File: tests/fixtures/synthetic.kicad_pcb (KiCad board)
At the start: 2 copper layers, 50 x 30 mm, 3 parts, among them U1 REG

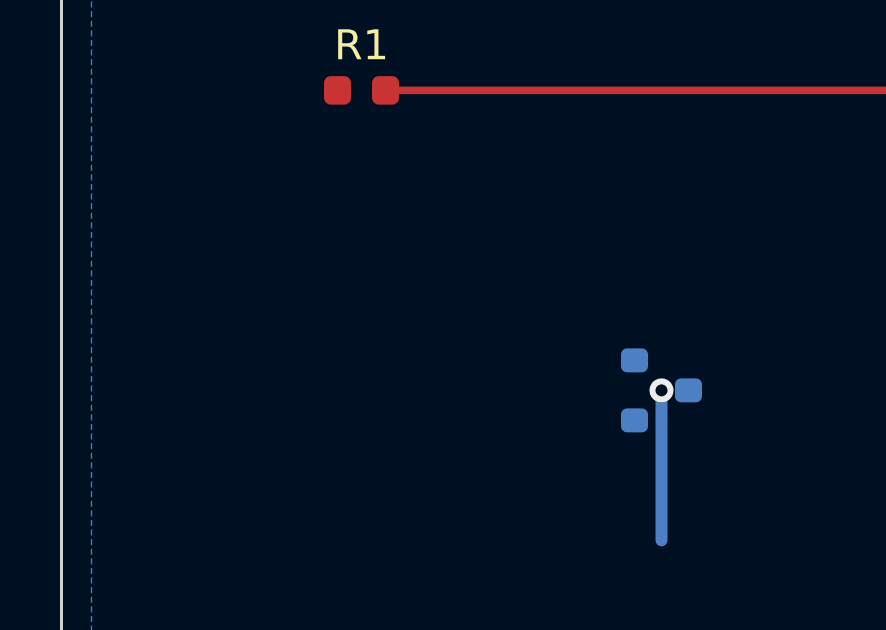
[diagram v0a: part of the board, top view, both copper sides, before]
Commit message: [Build] fix synthetic route fixture edits
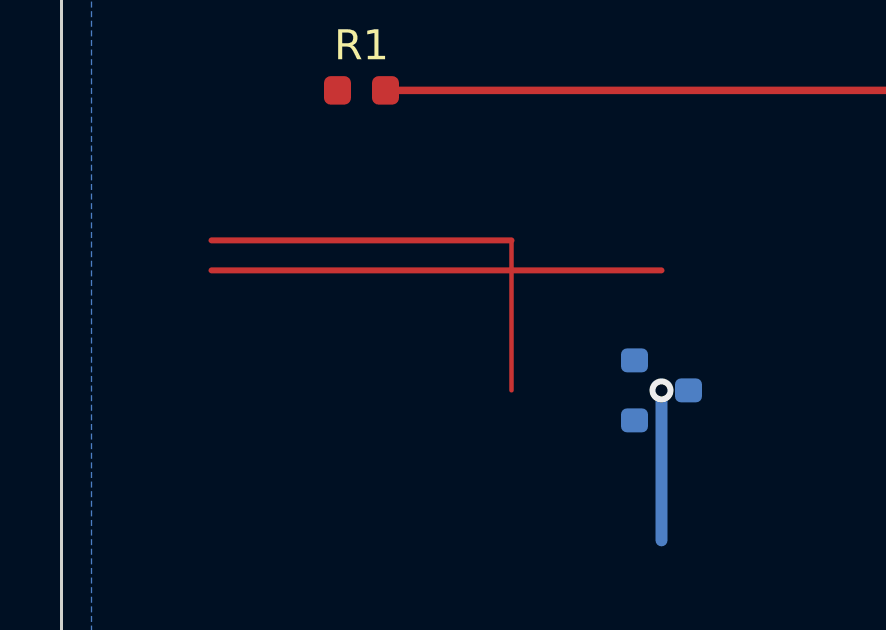
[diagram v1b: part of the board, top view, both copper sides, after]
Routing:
- net DP_P: track 0.00 -> 15.0 mm
- net DP_N: track 0.00 -> 15.0 mm
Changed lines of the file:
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@@
 	(net 2 "VCC")
 	(net 3 "SIG")
+	(net 4 "DP_P")
+	(net 5 "DP_N")
 	(footprint "Resistor_SMD:R_0603_1608Metric"
 		(layer "F.Cu")
@@
 		(net 1)
 	)
+	(segment
+		(start 105 115)
+		(end 115 115)
+		(width 0.2)
+		(layer "F.Cu")
+		(net 4)
+	)
+	(segment
+		(start 115 115)
+		(end 115 120)
+		(width 0.15)
+		(layer "F.Cu")
+		(net 4)
+	)
+	(segment
+		(start 105 116)
+		(end 120 116)
+		(width 0.2)
+		(layer "F.Cu")
+		(net 5)
+	)
 	(zone

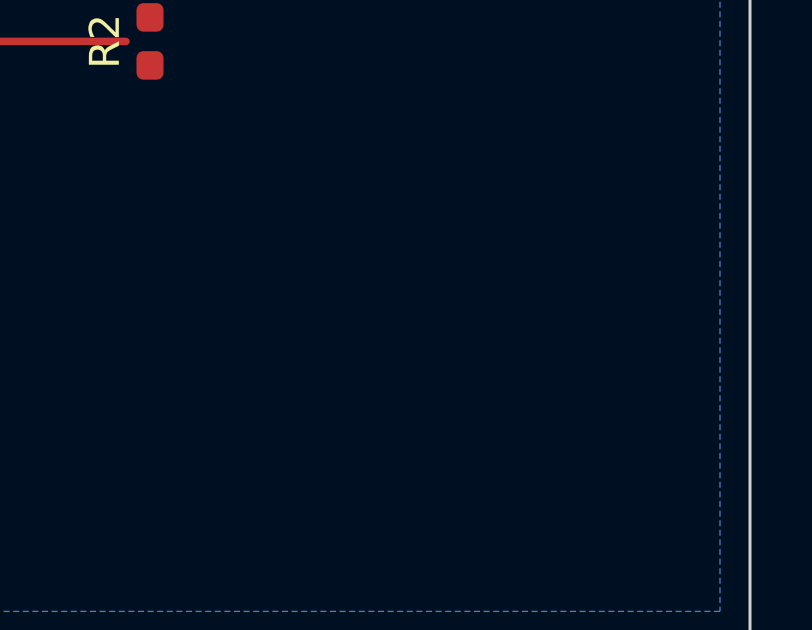
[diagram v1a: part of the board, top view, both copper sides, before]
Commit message: extend synthetic fixture with through-hole silk footprint
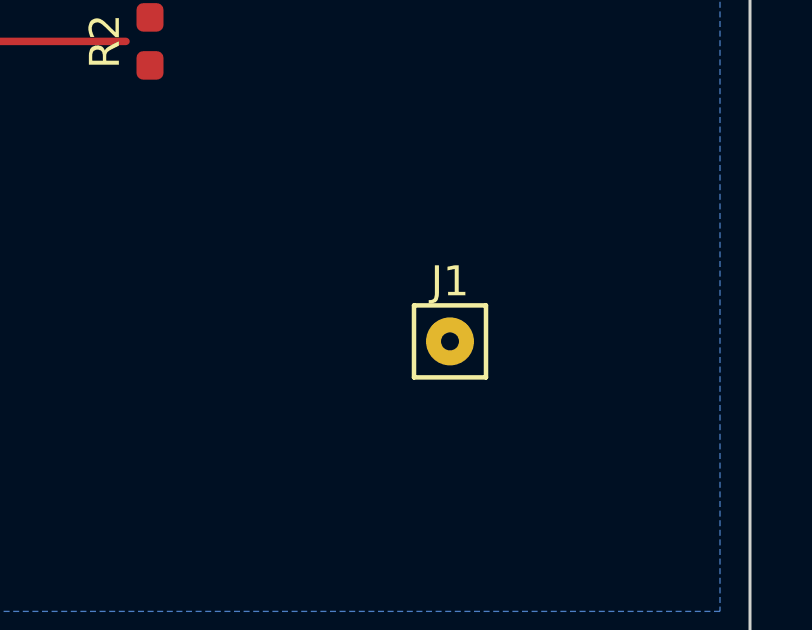
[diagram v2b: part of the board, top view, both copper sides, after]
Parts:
- added J1: TH, Connector_PinHeader_2.54mm:PinHeader_1x01_P2.54mm_Vertical, F.Cu at (140.0, 120.0)
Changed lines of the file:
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@@
+		)
+	)
+	(footprint "Connector_PinHeader_2.54mm:PinHeader_1x01_P2.54mm_Vertical"
+		(layer "F.Cu")
+		(at 140 120 0)
+		(property "Reference" "J1"
+			(at 0 -2 0)
+			(layer "F.SilkS")
+			(effects
+				(font
+					(size 1 1)
+					(thickness 0.15)
+				)
+			)
+		)
+		(property "Value" "TH"
+			(at 0 2 0)
+			(layer "F.Fab")
+			(effects
+				(font
+					(size 1 1)
+					(thickness 0.15)
+				)
+			)
+		)
+		(fp_line
+			(start -1.2 -1.2)
+			(end 1.2 -1.2)
+			(stroke
+				(width 0.15)
+				(type solid)
+			)
+			(layer "F.SilkS")
+		)
+		(fp_line
+			(start 1.2 -1.2)
+			(end 1.2 1.2)
+			(stroke
+				(width 0.15)
+				(type solid)
+			)
+			(layer "F.SilkS")
+		)
+		(fp_line
+			(start 1.2 1.2)
+			(end -1.2 1.2)
+			(stroke
+				(width 0.15)
+				(type solid)
+			)
+			(layer "F.SilkS")
+		)
+		(fp_line
+			(start -1.2 1.2)
+			(end -1.2 -1.2)
+			(stroke
+				(width 0.15)
+				(type solid)
+			)
+			(layer "F.SilkS")
+		)
+		(pad "1" thru_hole circle
+			(at 0 0)
+			(size 1.6 1.6)
+			(drill 0.6)
+			(layers "*.Cu" "*.Mask")
+			(net 1 "GND")
 		)
 	)
